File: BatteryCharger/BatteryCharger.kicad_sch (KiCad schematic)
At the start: 48 parts, among them J1 SYS, J2 ADAPTER, J3 BAT, J4 SMBus+STATUS, J5 GND_BRIDGE, J6 GND_BRIDGE, Q1 SiR638DP, Q2 SiR638DP, Q3 SiR500DP, Q4 BSC059N04LS6, Q5 SQJ868EP, U1 BQ24735, U2 NCP51460

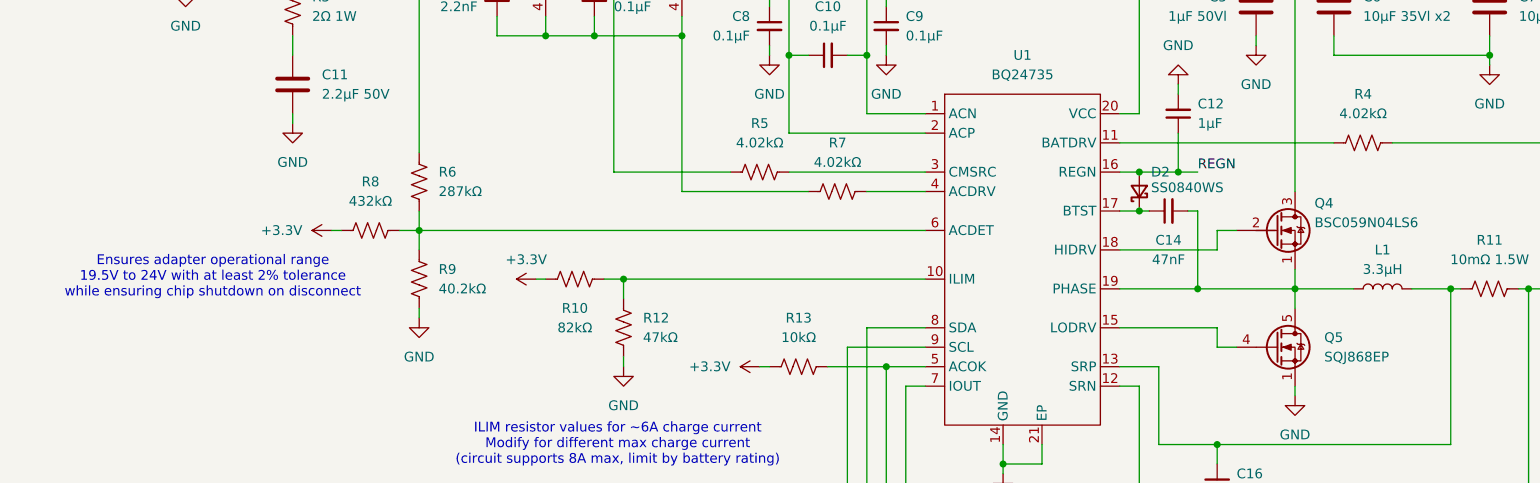
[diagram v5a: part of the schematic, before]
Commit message: BatteryCharger v1.2: Increased input voltage range
Now 17.5V min instead of 19.5V min, to avoid power cycling at startup due to inrush
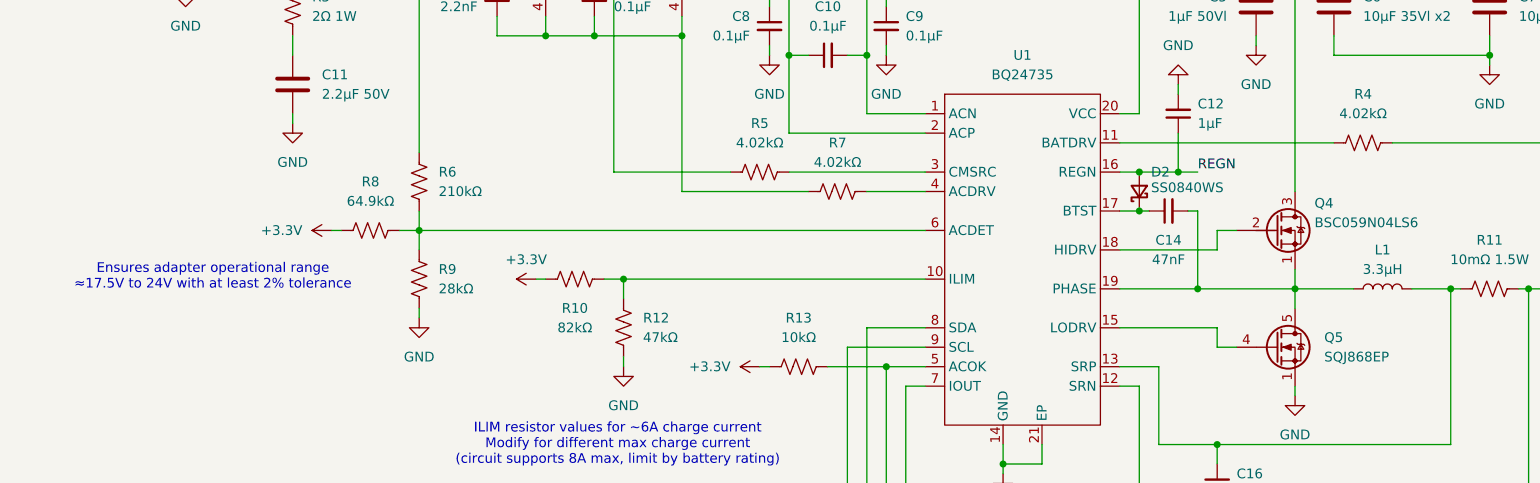
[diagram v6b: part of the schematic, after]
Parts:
- R6: value 287kΩ -> 210kΩ
- R8: value 432kΩ -> 64.9kΩ
- R9: value 40.2kΩ -> 28kΩ
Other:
- note added: "Ensures adapter operational range ≈17.5V to 24V with at least 2% tolerance"
- note removed: "Ensures adapter operational range 19.5V to 24V with at least 2% tolerance while ensuring chip shutdown on disconnect"
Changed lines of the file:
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@@
 (kicad_sch
-	(version 20231120)
+	(version 20250114)
 	(generator "eeschema")
-	(generator_version "8.0")
+	(generator_version "9.0")
 	(paper "A4")
+	(text "ILIM resistor values for ~6A charge current\nModify for different max charge current\n(circuit supports 8A max, limit by battery rating)"
+		(exclude_from_sim no)
+		(at 95.758 128.27 0)
+		(effects
+			(font
+				(size 1.27 1.27)
+			)
+		)
+	)
+	(text "May need to reduce C_{gs}\nIf turnon is too slow (>20ms)\nEnsure C_{gs} > 20 * C_{gd}"
+		(exclude_from_sim no)
+		(at 107.442 52.832 0)
+		(effects
+			(font
+				(size 1.27 1.27)
+			)
+		)
+	)
+	(text "Possible future addition:\nReverse polarity protection?"
+		(exclude_from_sim no)
+		(at 86.106 32.512 0)
+		(effects
+			(font
+				(size 1.27 1.27)
+			)
+		)
+	)
+	(text "Ensures adapter operational range\n≈17.5V to 24V with at least 2% tolerance"
+		(exclude_from_sim no)
+		(at 42.926 106.426 0)
+		(effects
+			(font
+				(size 1.27 1.27)
+			)
+		)
+	)
 	(junction
 		(at 118.11 64.77)
@@
 		)
 	)
-	(text "ILIM resistor values for ~6A charge current\nModify for different max charge current\n(circuit supports 8A max, limit by battery rating)"
-		(exclude_from_sim no)
-		(at 95.758 128.27 0)
-		(effects
-			(font
-				(size 1.27 1.27)
-			)
-		)
-	)
-	(text "May need to reduce C_{gs}\nIf turnon is too slow (>20ms)\nEnsure C_{gs} > 20 * C_{gd}"
-		(exclude_from_sim no)
-		(at 107.442 52.832 0)
-		(effects
-			(font
-				(size 1.27 1.27)
-			)
-		)
-	)
-	(text "Possible future addition:\nReverse polarity protection?"
-		(exclude_from_sim no)
-		(at 86.106 32.512 0)
-		(effects
-			(font
-				(size 1.27 1.27)
-			)
-		)
-	)
-	(text "Ensures adapter operational range\n19.5V to 24V with at least 2% tolerance\nwhile ensuring chip shutdown on disconnect"
-		(exclude_from_sim no)
-		(at 42.926 106.426 0)
-		(effects
-			(font
-				(size 1.27 1.27)
-			)
-		)
-	)
 	(label "REGN"
 		(at 171.45 92.71 0)
@@
 			)
 		)
-		(property "Value" "40.2kΩ"
+		(property "Value" "28kΩ"
 			(at 72.39 107.9499 0)
 			(effects
@@
 			)
 		)
-		(property "Value" "432kΩ"
+		(property "Value" "64.9kΩ"
 			(at 63.5 96.52 90)
 			(effects
@@
 			)
 		)
-		(property "Value" "287kΩ"
+		(property "Value" "210kΩ"
 			(at 72.39 95.2499 0)
 			(effects
@@
 		)
 	)
+	(embedded_fonts no)
 )
